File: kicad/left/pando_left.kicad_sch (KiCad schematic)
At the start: 87 parts, among them J1 USB_C_Receptacle_USB2.0_14P, J2 USB_C_Receptacle_USB2.0_14P, U1 STM32F072CBT6, U2 PRTR5V0U2X, U3 XC6206PxxxMR-Regulator_Linear, U4 PRTR5V0U2X

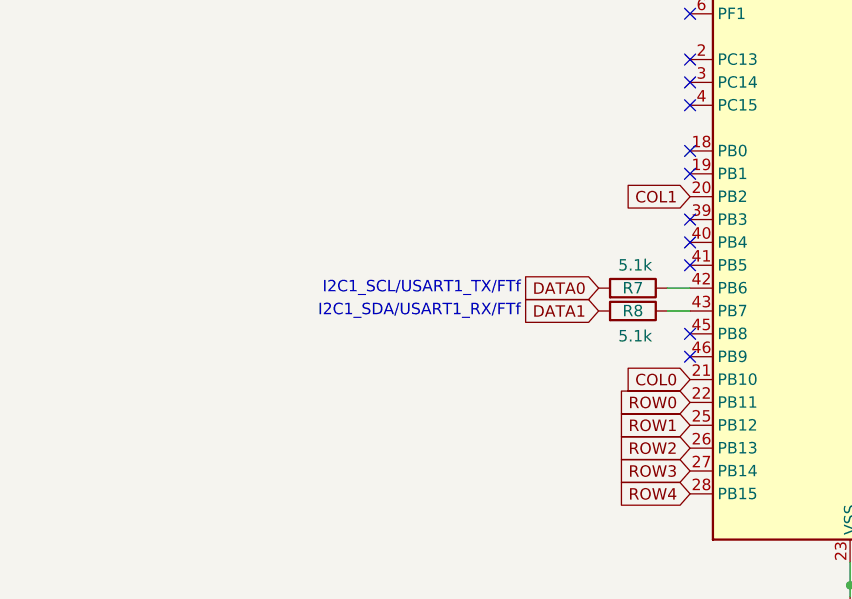
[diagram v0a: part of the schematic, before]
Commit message: v1.1.0: Fix I2C pull-up routing and clean up traces
- Reposition I2C pull-up resistors R7/R8 with VBUS connections
- Clean up DATA0/DATA1 label positions and wire routing
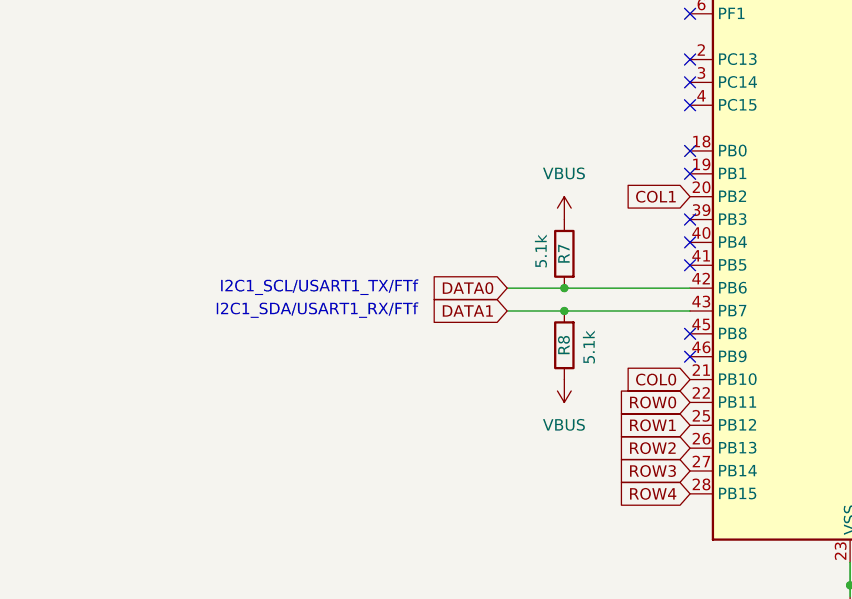
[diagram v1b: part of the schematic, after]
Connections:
- net DATA0: now also U1.42 (PB6)
- net DATA1: now also U1.43 (PB7)
- net VBUS: now also R7.1, R8.1
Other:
- moved on the sheet: R7, R8
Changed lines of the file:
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@@
 	(title_block
 		(title "Pando - Left PCB")
-		(rev "v1.0.0")
+		(date "2026-06-25")
+		(rev "v1.1.0")
 		(company "Julian Yap")
 	)
@@
 	(text "I2C1_SCL/USART1_TX/FTf"
 		(exclude_from_sim no)
-		(at 91.694 96.012 0)
+		(at 80.264 96.012 0)
 		(effects
 			(font
@@
 	(text "I2C1_SDA/USART1_RX/FTf"
 		(exclude_from_sim no)
-		(at 91.694 98.552 0)
+		(at 80.264 98.552 0)
 		(effects
 			(font
@@
 	)
 	(junction
+		(at 96.52 97.79)
+		(diameter 0)
+		(color 0 0 0 0)
+	)
+	(junction
 		(at 26.67 177.8)
 		(diameter 0)
@@
 	)
 	(junction
+		(at 96.52 95.25)
+		(diameter 0)
+		(color 0 0 0 0)
+	)
+	(junction
 		(at 222.25 212.09)
 		(diameter 0)
@@
 	(wire
 		(pts
+			(xy 90.17 97.79) (xy 96.52 97.79)
+		)
+		(stroke
+			(width 0)
+			(type default)
+		)
+	)
+	(wire
+		(pts
 			(xy 48.26 262.89) (xy 52.07 262.89)
 		)
@@
 	(wire
 		(pts
-			(xy 107.95 95.25) (xy 110.49 95.25)
-		)
-		(stroke
-			(width 0)
-			(type default)
-		)
-	)
-	(wire
-		(pts
 			(xy 318.77 92.71) (xy 318.77 115.57)
 		)
@@
 	(wire
 		(pts
-			(xy 107.95 97.79) (xy 110.49 97.79)
+			(xy 241.3 181.61) (xy 245.11 181.61)
 		)
 		(stroke
@@
 	(wire
 		(pts
-			(xy 241.3 181.61) (xy 245.11 181.61)
+			(xy 180.34 262.89) (xy 185.42 262.89)
 		)
 		(stroke
 			(width 0)
-			(type default)
+			(type solid)
 		)
 	)
 	(wire
 		(pts
-			(xy 180.34 262.89) (xy 185.42 262.89)
+			(xy 123.19 43.18) (xy 125.73 43.18)
 		)
 		(stroke
 			(width 0)
-			(type solid)
+			(type default)
 		)
 	)
 	(wire
 		(pts
-			(xy 123.19 43.18) (xy 125.73 43.18)
+			(xy 96.52 95.25) (xy 110.49 95.25)
 		)
 		(stroke
@@
 	(wire
 		(pts
+			(xy 96.52 97.79) (xy 110.49 97.79)
+		)
+		(stroke
+			(width 0)
+			(type default)
+		)
+	)
+	(wire
+		(pts
 			(xy 128.27 43.18) (xy 130.81 43.18)
 		)
@@
 	(wire
 		(pts
+			(xy 90.17 95.25) (xy 96.52 95.25)
+		)
+		(stroke
+			(width 0)
+			(type default)
+		)
+	)
+	(wire
+		(pts
 			(xy 254 175.26) (xy 257.81 175.26)
 		)
@@
 	(global_label "DATA0"
 		(shape input)
-		(at 100.33 95.25 180)
+		(at 90.17 95.25 180)
 		(fields_autoplaced yes)
 		(effects
@@
 		)
 		(property "Intersheetrefs" "${INTERSHEET_REFS}"
-			(at 89.5434 95.25 0)
+			(at 81.5605 95.25 0)
 			(hide yes)
 			(show_name no)
@@
 	(global_label "DATA1"
 		(shape input)
-		(at 100.33 97.79 180)
+		(at 90.17 97.79 180)
 		(fields_autoplaced yes)
 		(effects
@@
 		)
 		(property "Intersheetrefs" "${INTERSHEET_REFS}"
-			(at 89.241 97.79 0)
+			(at 81.5605 97.79 0)
 			(hide yes)
 			(show_name no)
@@
 	(symbol
 		(lib_id "Device:R")
-		(at 104.14 97.79 270)
-		(mirror x)
+		(at 96.52 101.6 180)
 		(unit 1)
 		(body_style 1)
@@
 		(dnp no)
 		(property "Reference" "R8"
-			(at 104.14 97.79 90)
+			(at 96.52 101.6 90)
 			(show_name no)
 			(do_not_autoplace no)
@@
 		)
 		(property "Value" "5.1k"
-			(at 104.394 100.584 90)
+			(at 99.314 101.854 90)
 			(show_name no)
 			(do_not_autoplace no)
@@
 		)
 		(property "Footprint" "Resistor_SMD:R_0603_1608Metric"
-			(at 104.14 99.568 90)
+			(at 98.298 101.6 90)
 			(hide yes)
 			(show_name no)
@@
 		)
 		(property "Datasheet" ""
-			(at 104.14 97.79 0)
+			(at 96.52 101.6 0)
 			(hide yes)
 			(show_name no)
@@
 		)
 		(property "Description" ""
-			(at 104.14 97.79 0)
+			(at 96.52 101.6 0)
 			(show_name no)
 			(do_not_autoplace no)
@@
 		)
 		(property "LCSC" "C2907114"
-			(at 104.14 97.79 90)
+			(at 96.52 101.6 90)
 			(hide yes)
 			(show_name no)
@@
 	(symbol
 		(lib_id "Device:R")
-		(at 104.14 95.25 270)
-		(mirror x)
+		(at 96.52 91.44 0)
+		(mirror y)
 		(unit 1)
 		(body_style 1)
@@
 		(dnp no)
 		(property "Reference" "R7"
-			(at 104.14 95.25 90)
+			(at 96.52 91.44 90)
 			(show_name no)
 			(do_not_autoplace no)
@@
 		)
 		(property "Value" "5.1k"
-			(at 104.394 92.71 90)
+			(at 93.98 91.186 90)
 			(show_name no)
 			(do_not_autoplace no)
@@
 		)
 		(property "Footprint" "Resistor_SMD:R_0603_1608Metric"
-			(at 104.14 97.028 90)
+			(at 98.298 91.44 90)
 			(hide yes)
 			(show_name no)
@@
 		)
 		(property "Datasheet" ""
-			(at 104.14 95.25 0)
+			(at 96.52 91.44 0)
 			(hide yes)
 			(show_name no)
@@
 		)
 		(property "Description" ""
-			(at 104.14 95.25 0)
+			(at 96.52 91.44 0)
 			(show_name no)
 			(do_not_autoplace no)
@@
 		)
 		(property "LCSC" "C2907114"
-			(at 104.14 95.25 90)
+			(at 96.52 91.44 90)
 			(hide yes)
 			(show_name no)
@@
 	)
 	(symbol
+		(lib_id "power:VBUS")
+		(at 96.52 87.63 0)
+		(unit 1)
+		(body_style 1)
+		(exclude_from_sim no)
+		(in_bom yes)
+		(on_board yes)
+		(in_pos_files yes)
+		(dnp no)
+		(fields_autoplaced yes)
+		(property "Reference" "#PWR026"
+			(at 96.52 91.44 0)
+			(hide yes)
+			(show_name no)
+			(do_not_autoplace no)
+			(effects
+				(font
+					(size 1.27 1.27)
+				)
+			)
+		)
+		(property "Value" "VBUS"
+			(at 96.52 82.55 0)
+			(show_name no)
+			(do_not_autoplace no)
+			(effects
+				(font
+					(size 1.27 1.27)
+				)
+			)
+		)
+		(property "Footprint" ""
+			(at 96.52 87.63 0)
+			(hide yes)
+			(show_name no)
+			(do_not_autoplace no)
+			(effects
+				(font
+					(size 1.27 1.27)
+				)
+			)
+		)
+		(property "Datasheet" ""
+			(at 96.52 87.63 0)
+			(hide yes)
+			(show_name no)
+			(do_not_autoplace no)
+			(effects
+				(font
+					(size 1.27 1.27)
+				)
+			)
+		)
+		(property "Description" "Power symbol creates a global label with name \"VBUS\""
+			(at 96.52 87.63 0)
+			(hide yes)
+			(show_name no)
+			(do_not_autoplace no)
+			(effects
+				(font
+					(size 1.27 1.27)
+				)
+			)
+		)
+		(pin "1"
+		)
+		(instances
+			(project "pando_left"
+				(path "/ed461b4e-82d7-439c-8b6c-f2725ca96a6c"
+					(reference "#PWR026")
+					(unit 1)
+				)
+			)
+		)
+	)
+	(symbol
 		(lib_id "Diode:1N4148W")
 		(at 307.34 101.6 90)
@@
 					(unit 1)
 				)
+			)
+		)
+	)
+	(symbol
+		(lib_id "power:VBUS")
+		(at 96.52 105.41 180)
+		(unit 1)
+		(body_style 1)
+		(exclude_from_sim no)
+		(in_bom yes)
+		(on_board yes)
+		(in_pos_files yes)
+		(dnp no)
+		(fields_autoplaced yes)
+		(property "Reference" "#PWR027"
+			(at 96.52 101.6 0)
+			(hide yes)
+			(show_name no)
+			(do_not_autoplace no)
+			(effects
+				(font
+					(size 1.27 1.27)
+				)
+			)
+		)
+		(property "Value" "VBUS"
+			(at 96.52 110.49 0)
+			(show_name no)
+			(do_not_autoplace no)
+			(effects
+				(font
+					(size 1.27 1.27)
+				)
+			)
+		)
+		(property "Footprint" ""
+			(at 96.52 105.41 0)
+			(hide yes)
+			(show_name no)
+			(do_not_autoplace no)
+			(effects
+				(font
+					(size 1.27 1.27)
+				)
+			)
+		)
+		(property "Datasheet" ""
+			(at 96.52 105.41 0)
+			(hide yes)
+			(show_name no)
+			(do_not_autoplace no)
+			(effects
+				(font
+					(size 1.27 1.27)
+				)
+			)
+		)
+		(property "Description" "Power symbol creates a global label with name \"VBUS\""
+			(at 96.52 105.41 0)
+			(hide yes)
+			(show_name no)
+			(do_not_autoplace no)
+			(effects
+				(font
+					(size 1.27 1.27)
+				)
+			)
+		)
+		(pin "1"
+		)
+		(instances
+			(project "pando_left"
+				(path "/ed461b4e-82d7-439c-8b6c-f2725ca96a6c"
+					(reference "#PWR027")
+					(unit 1)
+				)

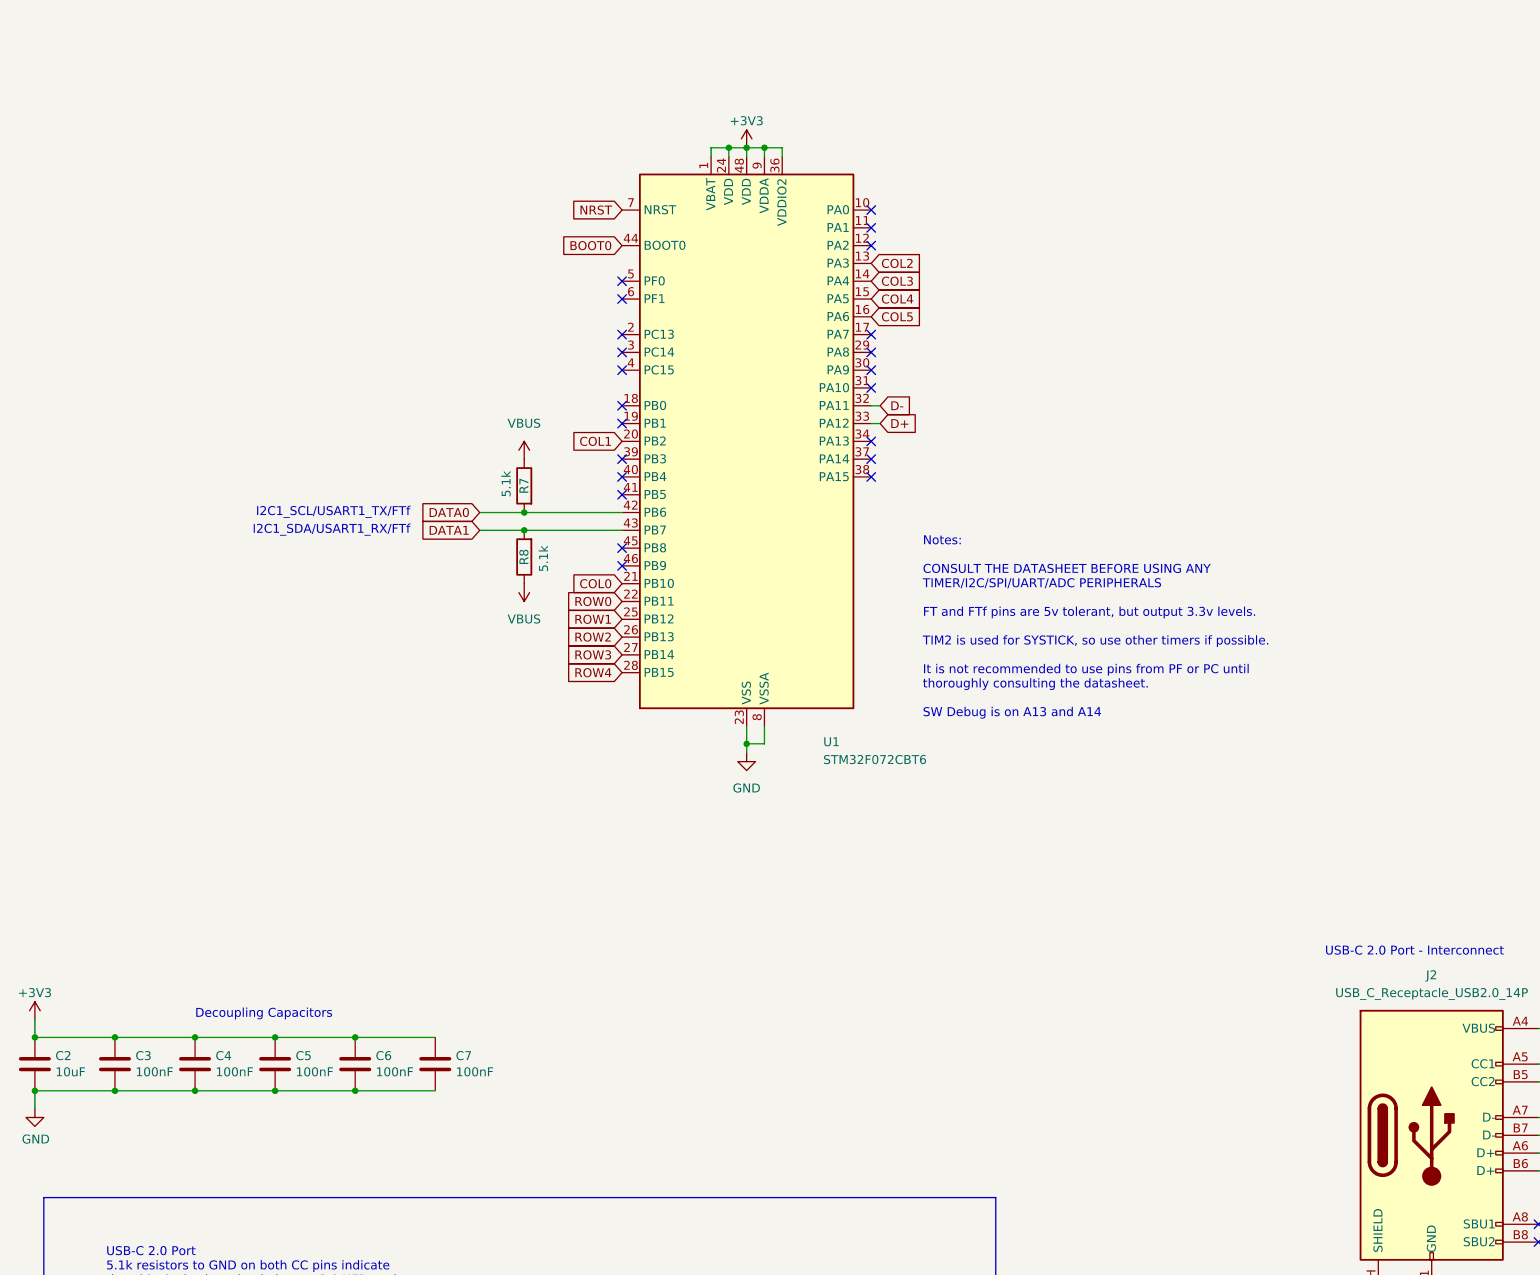
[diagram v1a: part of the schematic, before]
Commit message: Update left PCB and schematic for STM32G0B1CBT6
Replace STM32F072CBT6 with STM32G0B1CBT6 MCU. Update routing
and schematics to match new pinout and requirements.
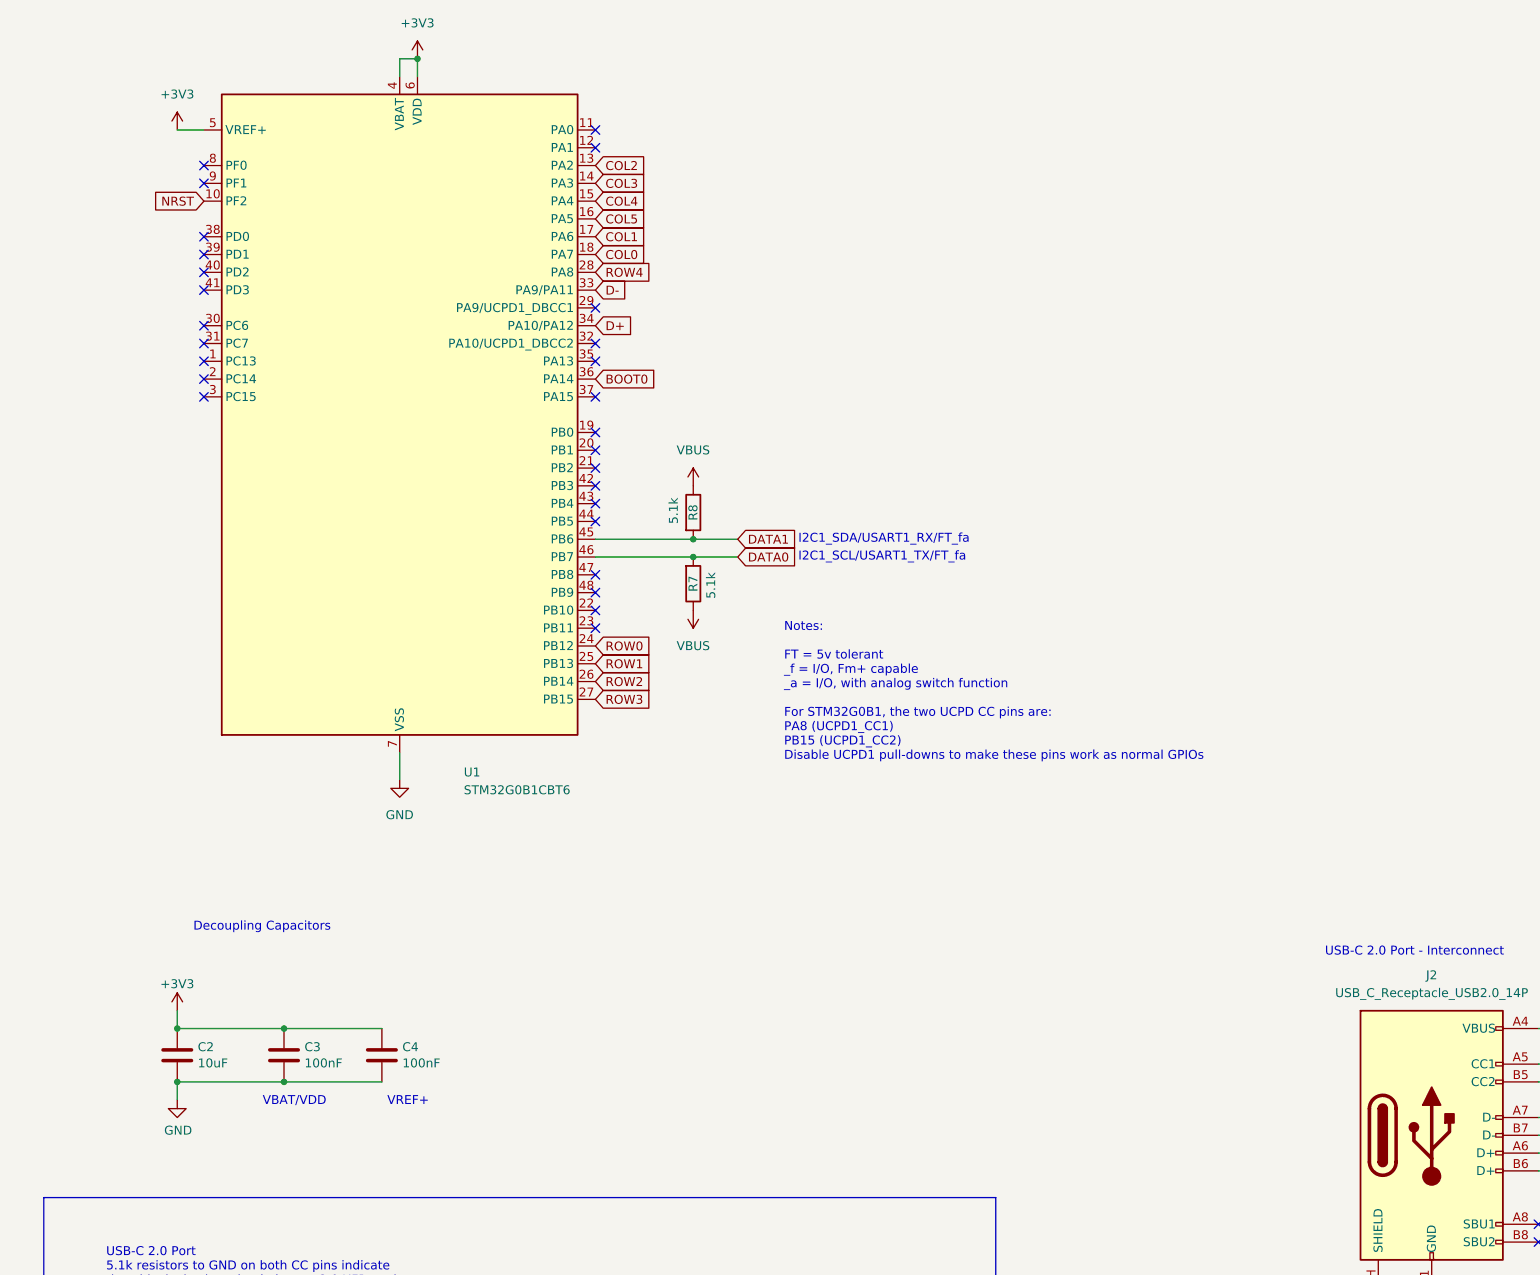
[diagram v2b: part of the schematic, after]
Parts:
- removed C5, C6, C7: 100nF, Capacitor_SMD:C_0603_1608Metric, symbol Device:C
- removed U1: STM32F072CBT6, Package_QFP:LQFP-48_7x7mm_P0.5mm, symbol MCU_ST_STM32F0:STM32F072CBTx
- added U1: STM32G0B1CBT6, Package_QFP:LQFP-48_7x7mm_P0.5mm, symbol MCU_ST_STM32G0:STM32G0B1CBTx
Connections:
- net +3V3: now also U1.4 (VBAT), U1.5 (VREF+), U1.6 (VDD)
- net BOOT0: now also U1.36 (PA14)
- net COL0: now also U1.18 (PA7)
- net COL1: now also U1.17 (PA6)
- net COL2: now also U1.13 (PA2)
- net COL3: now also U1.14 (PA3)
- net COL4: now also U1.15 (PA4)
- net COL5: now also U1.16 (PA5)
- net D+: now also U1.34 (PA10/PA12)
- net D-: now also U1.33 (PA9/PA11)
- net DATA0: now also U1.46 (PB7)
- net DATA1: now also U1.45 (PB6)
- net GND: now also U1.7 (VSS)
- net NRST: now also U1.10 (PF2)
- net ROW0: now also U1.24 (PB12)
- net ROW1: now also U1.25 (PB13)
- net ROW2: now also U1.26 (PB14)
- net ROW3: now also U1.27 (PB15)
- net ROW4: now also U1.28 (PA8)
- no-connect marks 26 -> 31
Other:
- note added: "I2C1_SCL/USART1_TX/FT_fa"
- note added: "I2C1_SDA/USART1_RX/FT_fa"
- note added: "Notes: FT = 5v tolerant _f = I/O, Fm+ capable _a = I/O, with analog switch function For STM32G0B1, the two UCPD CC pins are: PA8 (UCPD1_CC1) PB15 (UCPD1_CC2) Disable UCPD1 pull-downs to make these pins work as normal GPIOs"
- note added: "VBAT/VDD"
- note added: "VREF+"
- note removed: "I2C1_SCL/USART1_TX/FTf"
- note removed: "I2C1_SDA/USART1_RX/FTf"
- note removed: "Notes: CONSULT THE DATASHEET BEFORE USING ANY TIMER/I2C/SPI/UART/ADC PERIPHERALS FT and FTf pins are 5v tolerant, but output 3.3v levels. TIM2 is used for SYSTICK, so use other timers if possible. It is not recommended to use pins from PF or PC until thoroughly consulting the datasheet. SW Debug is on A13 and A14"
